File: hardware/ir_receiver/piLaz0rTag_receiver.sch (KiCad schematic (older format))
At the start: 4 parts, among them U1 TSOP4838

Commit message: Some rework on the ir receiver pcb
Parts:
- LED1: footprint LEDs:LED_D5.0mm-4 -> Socket_Strips:Socket_Strip_Straight_1x04_Pitch2.54mm
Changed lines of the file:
@@
 LIBS:contrib
 LIBS:valves
-LIBS:rur
-LIBS:ws2812b
+LIBS:pl8923
 LIBS:piLaz0rTag_receiver-cache
 EELAYER 25 0
@@
 F 0 "LED1" H 4200 750 60  0000 C CNN
 F 1 "PL8923" H 4200 1550 60  0000 C CNN
-F 2 "LEDs:LED_D5.0mm-4" V 4150 1150 60  0001 C CNN
+F 2 "Socket_Strips:Socket_Strip_Straight_1x04_Pitch2.54mm" V 4150 1150 60  0001 C CNN
 F 3 "" V 4150 1150 60  0000 C CNN
 	1    4200 1150

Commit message: #9 Ir Receiver
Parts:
- renumbered U1 to IR_REC1
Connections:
- net IR_DATA: now reaches IR_REC1.1 (OUT), Input1.4 (P4), Output1.4 (P4)
- net GND: now reaches IR_REC1.2 (GND), Input1.3 (P3), LED1.2 (GND), Output1.3 (P3)
- net +5V: now reaches IR_REC1.3 (Vs), Input1.1 (P1), LED1.3 (VCC), Output1.1 (P1)
- net LED_DIN: now reaches Input1.5 (P5), LED1.4 (DIN)
- net LED_DOUT: now reaches LED1.1 (DOUT), Output1.5 (P5)
- no-connect marks 0 -> 2
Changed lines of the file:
@@
 $EndDescr
 $Comp
-L TSOP4838 U1
+L TSOP4838 IR_REC1
 U 1 1 58F39155
 P 3400 2850
-F 0 "U1" H 3300 2600 60  0000 C CNN
+F 0 "IR_REC1" H 3300 2600 60  0000 C CNN
 F 1 "TSOP4838" H 3450 3100 60  0000 C CNN
 F 2 "Opto-Devices:IRReceiver_Vishay_MOLD-3pin" H 3400 2850 60  0001 C CNN
@@
 	1    0    0    -1
 $EndComp
-Wire Wire Line
-	1650 1750 1100 1750
-Wire Wire Line
-	1100 950  1100 3700
-Wire Wire Line
-	1100 950  3700 950
-Wire Wire Line
-	1850 1750 1850 3900
-Wire Wire Line
-	1850 1900 4700 1900
-Wire Wire Line
-	4700 1900 4700 1350
-Wire Wire Line
-	1850 2950 2950 2950
-Connection ~ 1850 1900
-Wire Wire Line
-	1100 2750 2950 2750
-Connection ~ 1100 1750
-Wire Wire Line
-	1100 3700 2450 3700
-Connection ~ 1100 2750
-Wire Wire Line
-	1850 3900 2450 3900
-Connection ~ 1850 2950
 Wire Wire Line
 	1950 1750 1950 4000
@@
 	1    0    0    -1
 $EndComp
+NoConn ~ 1750 1750
+NoConn ~ 2450 3800
+$Comp
+L GND #PWR01
+U 1 1 590CA84F
+P 2450 3900
+F 0 "#PWR01" H 2450 3650 50  0001 C CNN
+F 1 "GND" H 2450 3750 50  0000 C CNN
+F 2 "" H 2450 3900 50  0001 C CNN
+F 3 "" H 2450 3900 50  0001 C CNN
+	1    2450 3900
+	0    1    1    0
+$EndComp
+$Comp
+L GND #PWR02
+U 1 1 590CA8D5
+P 2950 2950
+F 0 "#PWR02" H 2950 2700 50  0001 C CNN
+F 1 "GND" H 2950 2800 50  0000 C CNN
+F 2 "" H 2950 2950 50  0001 C CNN
+F 3 "" H 2950 2950 50  0001 C CNN
+	1    2950 2950
+	0    1    1    0
+$EndComp
+$Comp
+L GND #PWR03
+U 1 1 590CA905
+P 4700 1350
+F 0 "#PWR03" H 4700 1100 50  0001 C CNN
+F 1 "GND" H 4700 1200 50  0000 C CNN
+F 2 "" H 4700 1350 50  0001 C CNN
+F 3 "" H 4700 1350 50  0001 C CNN
+	1    4700 1350
+	0    -1   -1   0
+$EndComp
+$Comp
+L GND #PWR04
+U 1 1 590CA921
+P 1850 1750
+F 0 "#PWR04" H 1850 1500 50  0001 C CNN
+F 1 "GND" H 1850 1600 50  0000 C CNN
+F 2 "" H 1850 1750 50  0001 C CNN
+F 3 "" H 1850 1750 50  0001 C CNN
+	1    1850 1750
+	1    0    0    -1
+$EndComp
+$Comp
+L +5V #PWR05
+U 1 1 590CA9D7
+P 1650 1750
+F 0 "#PWR05" H 1650 1600 50  0001 C CNN
+F 1 "+5V" H 1650 1890 50  0000 C CNN
+F 2 "" H 1650 1750 50  0001 C CNN
+F 3 "" H 1650 1750 50  0001 C CNN
+	1    1650 1750
+	-1   0    0    1
+$EndComp
+$Comp
+L +5V #PWR06
+U 1 1 590CAA28
+P 2450 3700
+F 0 "#PWR06" H 2450 3550 50  0001 C CNN
+F 1 "+5V" H 2450 3840 50  0000 C CNN
+F 2 "" H 2450 3700 50  0001 C CNN
+F 3 "" H 2450 3700 50  0001 C CNN
+	1    2450 3700
+	0    -1   -1   0
+$EndComp
+$Comp
+L +5V #PWR07
+U 1 1 590CAA44
+P 3700 950
+F 0 "#PWR07" H 3700 800 50  0001 C CNN
+F 1 "+5V" H 3700 1090 50  0000 C CNN
+F 2 "" H 3700 950 50  0001 C CNN
+F 3 "" H 3700 950 50  0001 C CNN
+	1    3700 950
+	0    -1   -1   0
+$EndComp
+$Comp
+L +5V #PWR08
+U 1 1 590CAAB3
+P 2950 2750
+F 0 "#PWR08" H 2950 2600 50  0001 C CNN
+F 1 "+5V" H 2950 2890 50  0000 C CNN
+F 2 "" H 2950 2750 50  0001 C CNN
+F 3 "" H 2950 2750 50  0001 C CNN
+	1    2950 2750
+	0    -1   -1   0
+$EndComp
+Text Label 2050 1750 0    60   ~ 0
+LED_DIN
+Text Label 2450 4100 2    60   ~ 0
+LED_DOUT
+Text Label 2950 2850 2    60   ~ 0
+IR_DATA
 $EndSCHEMATC

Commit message: Some minor changes on the receiver mainboard
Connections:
- net GND: now also Input1.2 (P2), Output1.2 (P2)
- no-connect marks 2 -> 0
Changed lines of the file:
@@
 	1    0    0    -1
 $EndComp
-NoConn ~ 1750 1750
-NoConn ~ 2450 3800
 $Comp
 L GND #PWR01
@@
 Text Label 2950 2850 2    60   ~ 0
 IR_DATA
+$Comp
+L GND #PWR?
+U 1 1 590DBFD1
+P 2450 3800
+F 0 "#PWR?" H 2450 3550 50  0001 C CNN
+F 1 "GND" H 2450 3650 50  0000 C CNN
+F 2 "" H 2450 3800 50  0001 C CNN
+F 3 "" H 2450 3800 50  0001 C CNN
+	1    2450 3800
+	0    1    1    0
+$EndComp
+$Comp
+L GND #PWR?
+U 1 1 590DBFED
+P 1750 1750
+F 0 "#PWR?" H 1750 1500 50  0001 C CNN
+F 1 "GND" H 1750 1600 50  0000 C CNN
+F 2 "" H 1750 1750 50  0001 C CNN
+F 3 "" H 1750 1750 50  0001 C CNN
+	1    1750 1750
+	1    0    0    -1
+$EndComp
 $EndSCHEMATC

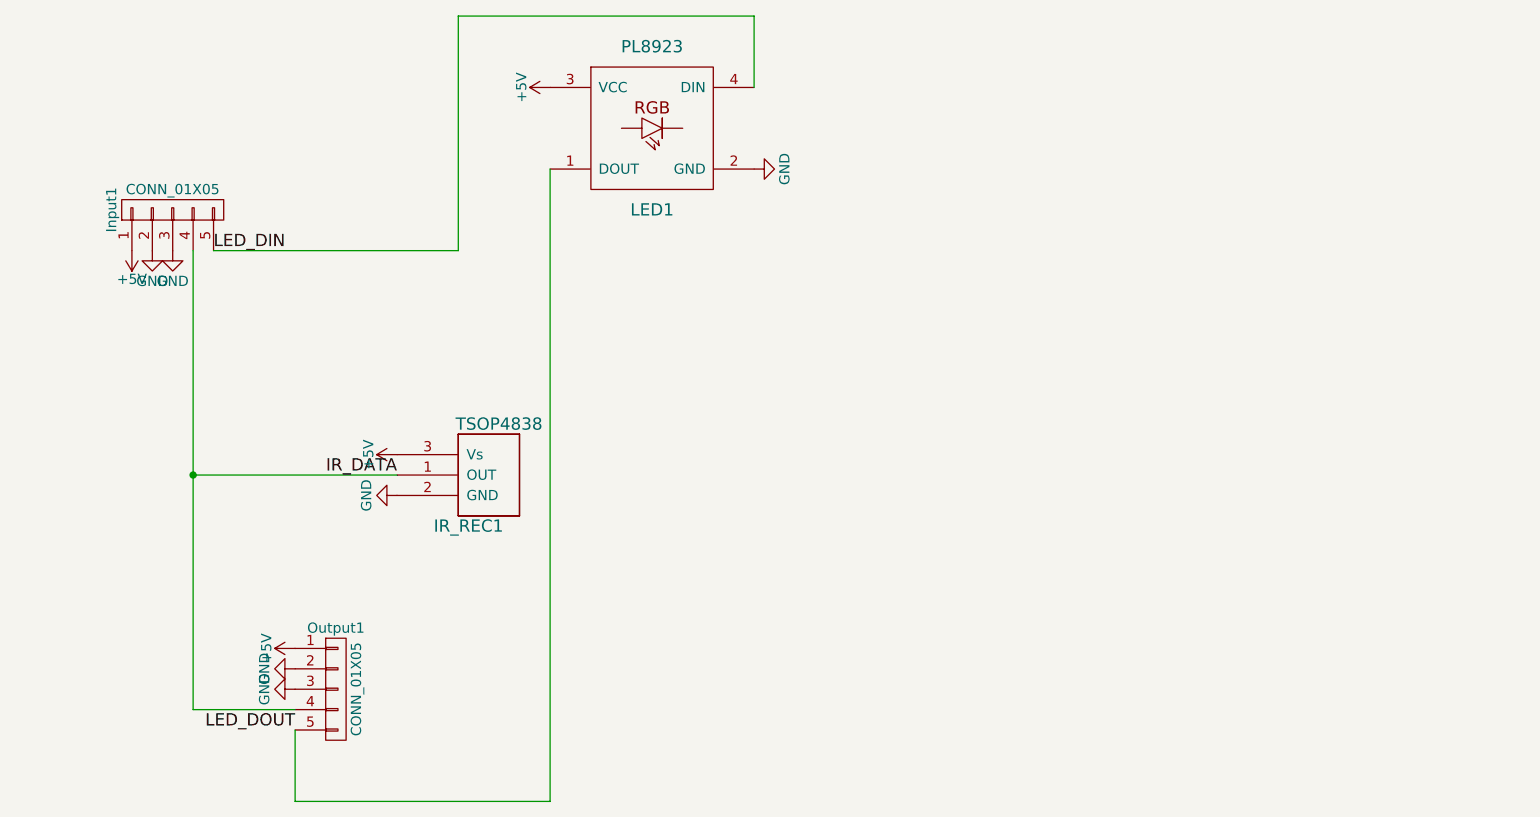
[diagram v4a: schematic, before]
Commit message: Start adding rj45 connectoren
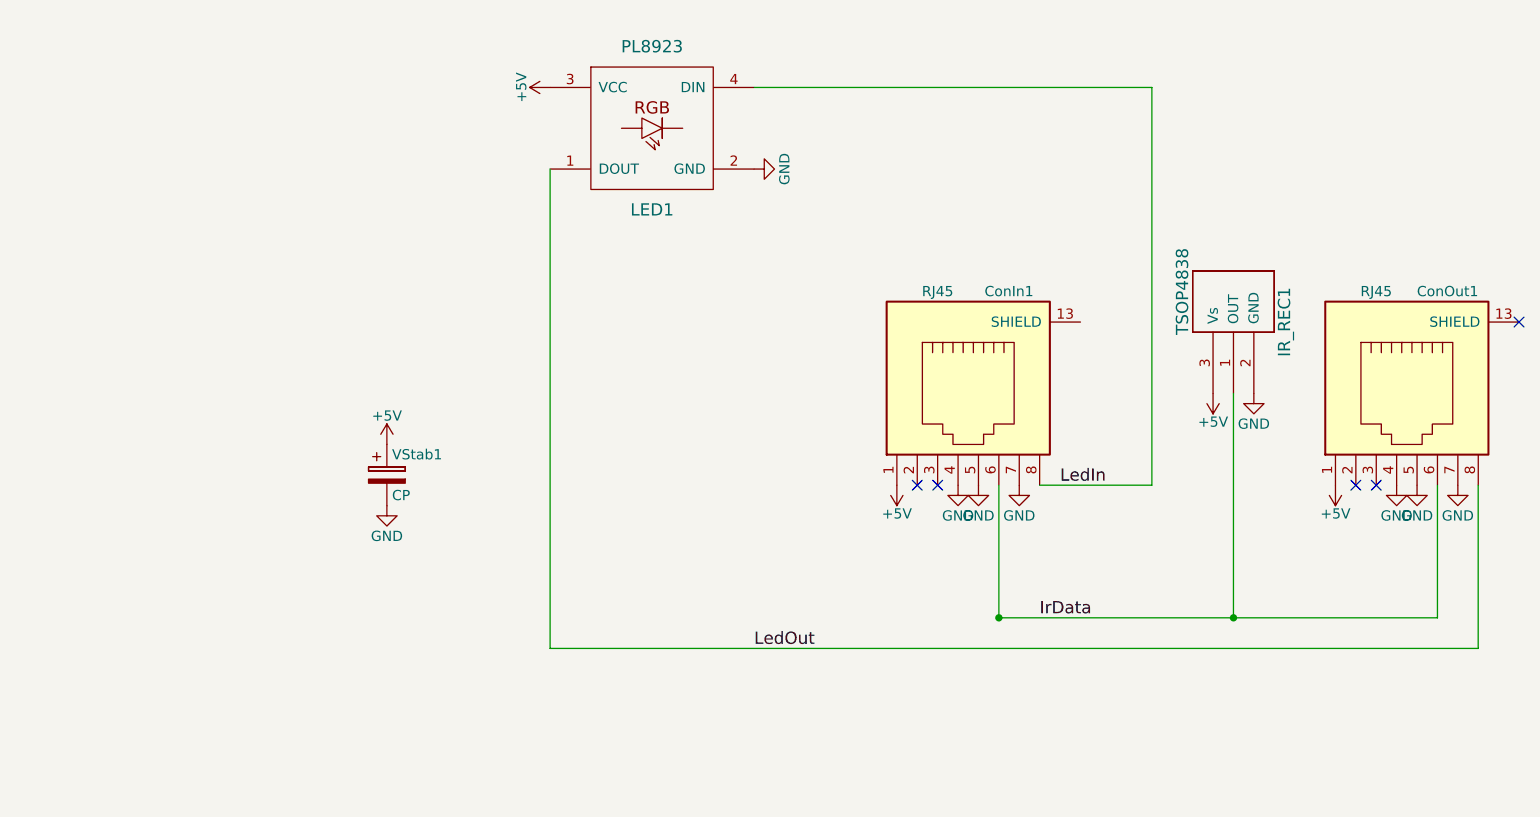
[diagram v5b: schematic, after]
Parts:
- removed Input1, Output1: CONN_01X05, Socket_Strips:Socket_Strip_Straight_1x05_Pitch2.54mm, symbol CONN_01X05
- added ConIn1, ConOut1: RJ45, kicad:rj45-seppel-small, symbol RJ45
- added VStab1: CP, Capacitors_THT:CP_Radial_D4.0mm_P2.00mm, symbol CP
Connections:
- net +5V: now also ConIn1.1, ConOut1.1, VStab1.1
- net GND: now also ConIn1.4, ConIn1.5, ConIn1.7, ConOut1.4, ConOut1.5, ConOut1.7, VStab1.2
- net IR_DATA renamed IrData
- net IrData: now also ConIn1.6, ConOut1.6
- net LED_DIN renamed LedIn
- net LedIn: now also ConIn1.8
- net LED_DOUT renamed LedOut
- net LedOut: now also ConOut1.8
- no-connect marks 0 -> 5
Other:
- moved on the sheet: IR_REC1

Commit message: More work on the receiver with rj45
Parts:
- ConIn1, ConOut1: symbol RJ45 -> RJ45-RESCUE-piLaz0rTag_receiver
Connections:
- net GND: no longer ConIn1.5, ConIn1.7, ConOut1.5, ConOut1.7
- no-connect marks 5 -> 9
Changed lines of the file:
@@
 $EndComp
 $Comp
-L RJ45 ConIn1
+L RJ45-RESCUE-piLaz0rTag_receiver ConIn1
 U 1 1 5AF828CC
 P 5750 2450
@@
 $EndComp
 $Comp
-L RJ45 ConOut1
+L RJ45-RESCUE-piLaz0rTag_receiver ConOut1
 U 1 1 5AF829C5
 P 7900 2450
@@
 $EndComp
 NoConn ~ 8450 2100
-$Comp
-L GND #PWR7
-U 1 1 5AF83492
-P 5800 2900
-F 0 "#PWR7" H 5800 2650 50  0001 C CNN
-F 1 "GND" H 5800 2750 50  0000 C CNN
-F 2 "" H 5800 2900 50  0001 C CNN
-F 3 "" H 5800 2900 50  0001 C CNN
-	1    5800 2900
-	1    0    0    -1
-$EndComp
-$Comp
-L GND #PWR8
-U 1 1 5AF834AE
-P 6000 2900
-F 0 "#PWR8" H 6000 2650 50  0001 C CNN
-F 1 "GND" H 6000 2750 50  0000 C CNN
-F 2 "" H 6000 2900 50  0001 C CNN
-F 3 "" H 6000 2900 50  0001 C CNN
-	1    6000 2900
-	1    0    0    -1
-$EndComp
-$Comp
-L GND #PWR13
-U 1 1 5AF834CA
-P 7950 2900
-F 0 "#PWR13" H 7950 2650 50  0001 C CNN
-F 1 "GND" H 7950 2750 50  0000 C CNN
-F 2 "" H 7950 2900 50  0001 C CNN
-F 3 "" H 7950 2900 50  0001 C CNN
-	1    7950 2900
-	1    0    0    -1
-$EndComp
-$Comp
-L GND #PWR14
-U 1 1 5AF834E6
-P 8150 2900
-F 0 "#PWR14" H 8150 2650 50  0001 C CNN
-F 1 "GND" H 8150 2750 50  0000 C CNN
-F 2 "" H 8150 2900 50  0001 C CNN
-F 3 "" H 8150 2900 50  0001 C CNN
-	1    8150 2900
-	1    0    0    -1
-$EndComp
 Connection ~ 5900 3550
 NoConn ~ 7650 2900
@@
 	1    0    0    -1
 $EndComp
+NoConn ~ 6000 2900
+NoConn ~ 5800 2900
+NoConn ~ 8150 2900
+NoConn ~ 7950 2900
 $EndSCHEMATC
